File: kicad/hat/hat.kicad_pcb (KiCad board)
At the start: 2 copper layers, 65 x 56 mm, 5 parts, among them J1 GPIO

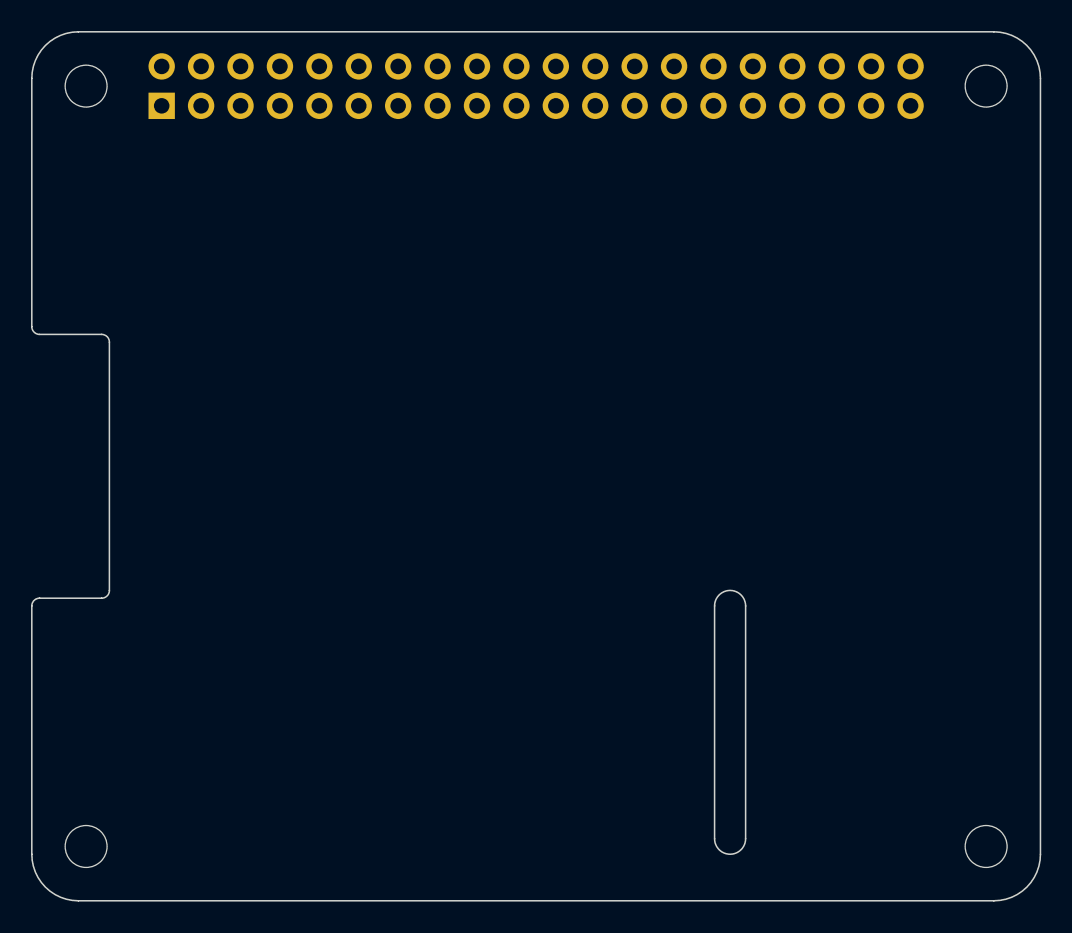
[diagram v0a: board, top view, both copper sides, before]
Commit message: addd pcb layer to hat
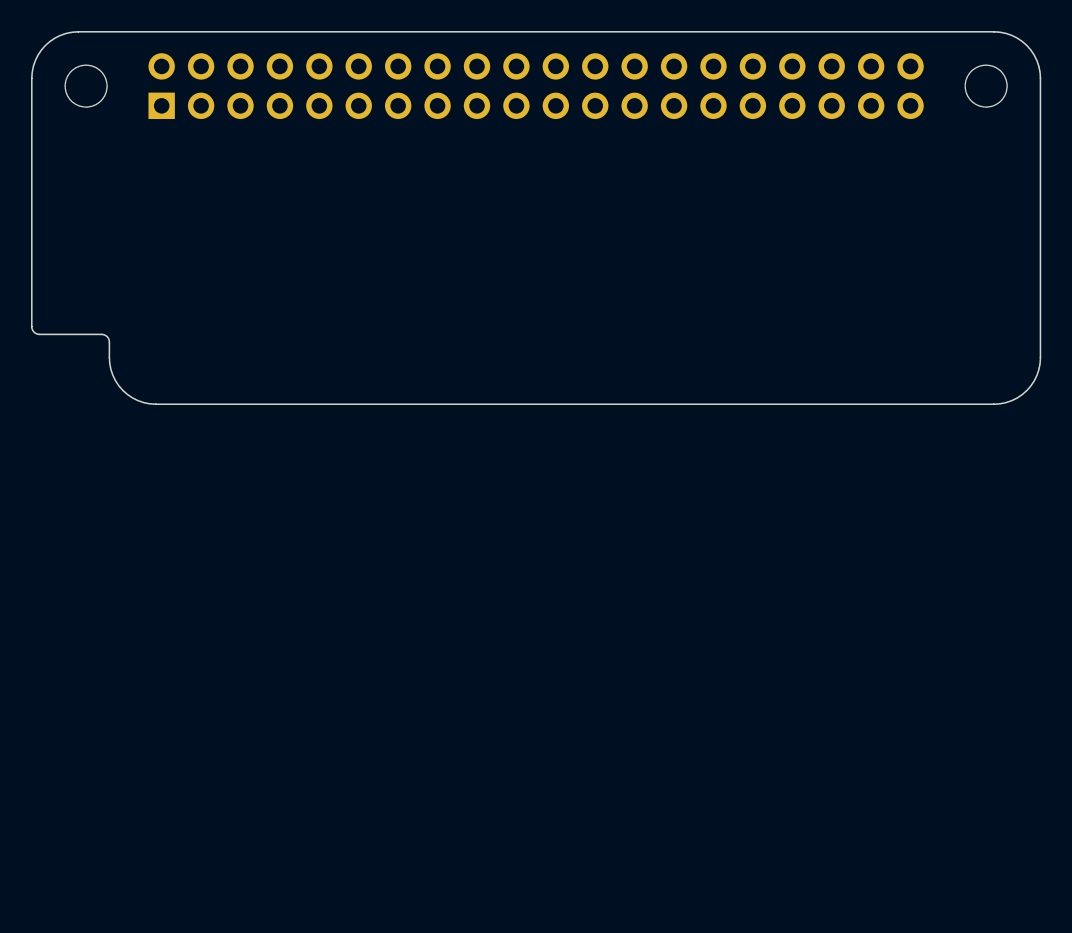
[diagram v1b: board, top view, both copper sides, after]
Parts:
- removed MH3, MH4: MountingHole_2.7mm_M2.5, MountingHole:MountingHole_2.7mm_M2.5
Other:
- board size 65 x 56 mm -> 65 x 24 mm
- board text removed: "CAMERA (OPTIONAL)"
- board text removed: "DISPLAY (OPTIONAL)"
